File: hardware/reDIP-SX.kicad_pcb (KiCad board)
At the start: 6 copper layers, 17.8 x 40.6 mm, 130 parts, among them J1 DX07S016JA3, J10 Conn_01x01, J11 Conn_01x01, J2 Conn_01x01, J3 Conn_01x01, J4 Conn_01x01, J5 Conn_01x06, J6 Conn_01x06, J7 Conn_01x10, J8 Conn_01x10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

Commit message: Renamed to reDIP SX
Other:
- board text added: "reDIP SX"
- board text removed: "reDIP"
- board text removed: "sx"
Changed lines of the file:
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@@
   (general
     (thickness 1.6)
-    (drawings 99)
+    (drawings 98)
     (tracks 2870)
     (zones 0)
@@
   (page A4 portrait)
   (title_block
-    (title "reDIP sx")
+    (title "reDIP SX")
     (date 2021-01-17)
     (rev 0.1)
@@
       (effects (font (size 1 1) (thickness 0.15)))
     )
-    (fp_text user %R (at 0 0 45) (layer F.Fab)
-      (effects (font (size 0.2 0.2) (thickness 0.03)))
-    )
     (fp_line (start -0.71 0.51) (end -0.71 0.26) (layer F.SilkS) (width 0.12))
     (fp_line (start -0.71 0.51) (end -0.46 0.51) (layer F.SilkS) (width 0.12))
@@
     (fp_line (start 0.51 -0.31) (end 0.51 0.31) (layer F.Fab) (width 0.1))
     (fp_line (start -0.31 -0.31) (end 0.51 -0.31) (layer F.Fab) (width 0.1))
+    (fp_text user %R (at 0 0 45) (layer F.Fab)
+      (effects (font (size 0.2 0.2) (thickness 0.03)))
+    )
     (pad "" smd roundrect (at 0.35 0 45) (size 0.3 0.6) (layers F.Paste) (roundrect_rratio 0.125))
     (pad "" smd roundrect (at -0.35 0.225 45) (size 0.3 0.25) (layers F.Paste) (roundrect_rratio 0.2))
@@
       (effects (font (size 1 1) (thickness 0.15)))
     )
-    (fp_text user %R (at 0 0 45) (layer F.Fab)
-      (effects (font (size 0.5 0.5) (thickness 0.075)))
-    )
     (fp_line (start 1.5 1.1) (end 1.5 -1.1) (layer F.CrtYd) (width 0.05))
     (fp_line (start -1.5 -1.1) (end -1.5 1.1) (layer F.CrtYd) (width 0.05))
@@
     (fp_line (start 0.6 -0.9) (end -1.1 -0.9) (layer F.SilkS) (width 0.12))
     (fp_line (start -0.6 -0.5) (end -0.3 -0.8) (layer F.Fab) (width 0.1))
+    (fp_text user %R (at 0 0 45) (layer F.Fab)
+      (effects (font (size 0.5 0.5) (thickness 0.075)))
+    )
     (pad 6 smd roundrect (at 0.85 -0.5375 315) (size 0.5 0.375) (layers F.Cu F.Paste F.Mask) (roundrect_rratio 0.25)
       (net 88 /ESP_EN))
@@
       (effects (font (size 1 1) (thickness 0.15)))
     )
-    (fp_text user %R (at 0 0 90) (layer F.Fab)
-      (effects (font (size 0.3 0.3) (thickness 0.06)))
-    )
     (fp_line (start -0.5 0.975) (end 0.5 0.975) (layer F.Fab) (width 0.1))
     (fp_line (start 0.5 -0.975) (end 0.5 0.975) (layer F.Fab) (width 0.1))
@@
     (fp_line (start -0.75 1.175) (end 0.75 1.175) (layer F.CrtYd) (width 0.05))
     (fp_line (start -0.75 -1.175) (end -0.75 1.175) (layer F.CrtYd) (width 0.05))
+    (fp_text user %R (at 0 0 90) (layer F.Fab)
+      (effects (font (size 0.3 0.3) (thickness 0.06)))
+    )
     (pad 2 smd roundrect (at -0.3375 -0.25 270) (size 0.4 0.3) (layers F.Cu F.Paste F.Mask) (roundrect_rratio 0.2)
       (net 47 /ICE_POT_X))
@@
       (effects (font (size 1 1) (thickness 0.15)))
     )
-    (fp_text user %R (at 0 0 90) (layer F.Fab)
-      (effects (font (size 0.3 0.3) (thickness 0.06)))
-    )
     (fp_line (start -1 1.2) (end -1 -1.2) (layer F.CrtYd) (width 0.05))
     (fp_line (start 1 1.2) (end -1 1.2) (layer F.CrtYd) (width 0.05))
@@
     (fp_line (start -0.7 -0.55) (end -0.7 0.9) (layer F.Fab) (width 0.1))
     (fp_line (start -0.35 -0.9) (end -0.7 -0.55) (layer F.Fab) (width 0.1))
+    (fp_text user %R (at 0 0 90) (layer F.Fab)
+      (effects (font (size 0.3 0.3) (thickness 0.06)))
+    )
     (pad 10 smd roundrect (at -0.4 -0.7685 90) (size 0.225 0.563) (layers F.Cu F.Paste F.Mask) (roundrect_rratio 0.25)
       (net 72 /D+))
@@
       (effects (font (size 1 1) (thickness 0.15)))
     )
-    (fp_text user %R (at 0 0) (layer F.Fab)
-      (effects (font (size 0.3 0.3) (thickness 0.06)))
-    )
     (fp_line (start -0.7 -1.85) (end -0.4 -1.85) (layer F.SilkS) (width 0.12))
     (fp_line (start 0.4 -1.85) (end 0.7 -1.85) (layer F.SilkS) (width 0.12))
@@
     (fp_line (start -0.4 1.85) (end -0.7 1.85) (layer F.SilkS) (width 0.12))
     (fp_line (start -0.7 1.85) (end -0.7 1.65) (layer F.SilkS) (width 0.12))
+    (fp_text user %R (at 0 0) (layer F.Fab)
+      (effects (font (size 0.3 0.3) (thickness 0.06)))
+    )
     (pad 1 smd roundrect (at -0.35 -1.4 180) (size 0.25 0.5) (layers F.Cu F.Paste F.Mask) (roundrect_rratio 0.2)
       (net 70 /SBU1))
@@
       (effects (font (size 1 1) (thickness 0.15)))
     )
-    (fp_text user %R (at 0 0) (layer F.Fab)
-      (effects (font (size 0.7 0.7) (thickness 0.1)))
-    )
     (fp_line (start -1.6 -0.8) (end -0.8 -1.59) (layer F.Fab) (width 0.1))
     (fp_line (start -2.25 2.25) (end 2.25 2.25) (layer F.CrtYd) (width 0.05))
@@
     (fp_line (start -1.92 -1.91) (end -2.07 -2.06) (layer F.SilkS) (width 0.12))
     (fp_line (start -2.07 -2.06) (end -1.45 -2.06) (layer F.SilkS) (width 0.12))
+    (fp_text user %R (at 0 0) (layer F.Fab)
+      (effects (font (size 0.7 0.7) (thickness 0.1)))
+    )
     (pad 1 smd roundrect (at -1.075 -1.075) (size 1.35 1.35) (layers F.Cu F.Paste F.Mask) (roundrect_rratio 0.05)
       (net 1 "Net-(AE1-Pad1)"))
@@
       (effects (font (size 1 1) (thickness 0.15)))
     )
-    (fp_text user %R (at 0 0 90) (layer F.Fab)
-      (effects (font (size 0.2 0.2) (thickness 0.04)))
-    )
     (fp_line (start -0.68 -0.68) (end -0.43 -0.68) (layer F.SilkS) (width 0.12))
     (fp_line (start 0.68 -0.43) (end 0.68 -0.68) (layer F.SilkS) (width 0.12))
@@
     (fp_line (start -0.75 0.75) (end 0.75 0.75) (layer F.CrtYd) (width 0.05))
     (fp_line (start -0.75 -0.75) (end 0.75 -0.75) (layer F.CrtYd) (width 0.05))
+    (fp_text user %R (at 0 0 90) (layer F.Fab)
+      (effects (font (size 0.2 0.2) (thickness 0.04)))
+    )
     (pad C3 smd circle (at 0.4 0.4 90) (size 0.2 0.2) (layers F.Cu F.Paste F.Mask)
       (net 2 GND))
@@
     (effects (font (size 1.1 1.1) (thickness 0.15)) (justify mirror))
   )
-  (gr_text sx (at 113.31 120.02 270) (layer F.SilkS)
-    (effects (font (size 1 1) (thickness 0.2)))
-  )
   (gr_text "© 2021" (at 102.6 125.51 90) (layer B.SilkS)
     (effects (font (size 0.8 0.8) (thickness 0.15)) (justify mirror))
@@
     (effects (font (size 0.8 0.8) (thickness 0.15)) (justify mirror))
   )
-  (gr_text reDIP (at 113.31 116.81 270) (layer F.SilkS)
+  (gr_text "reDIP SX" (at 113.32 117.63 -90) (layer F.SilkS)
     (effects (font (size 1 1) (thickness 0.2)))
   )

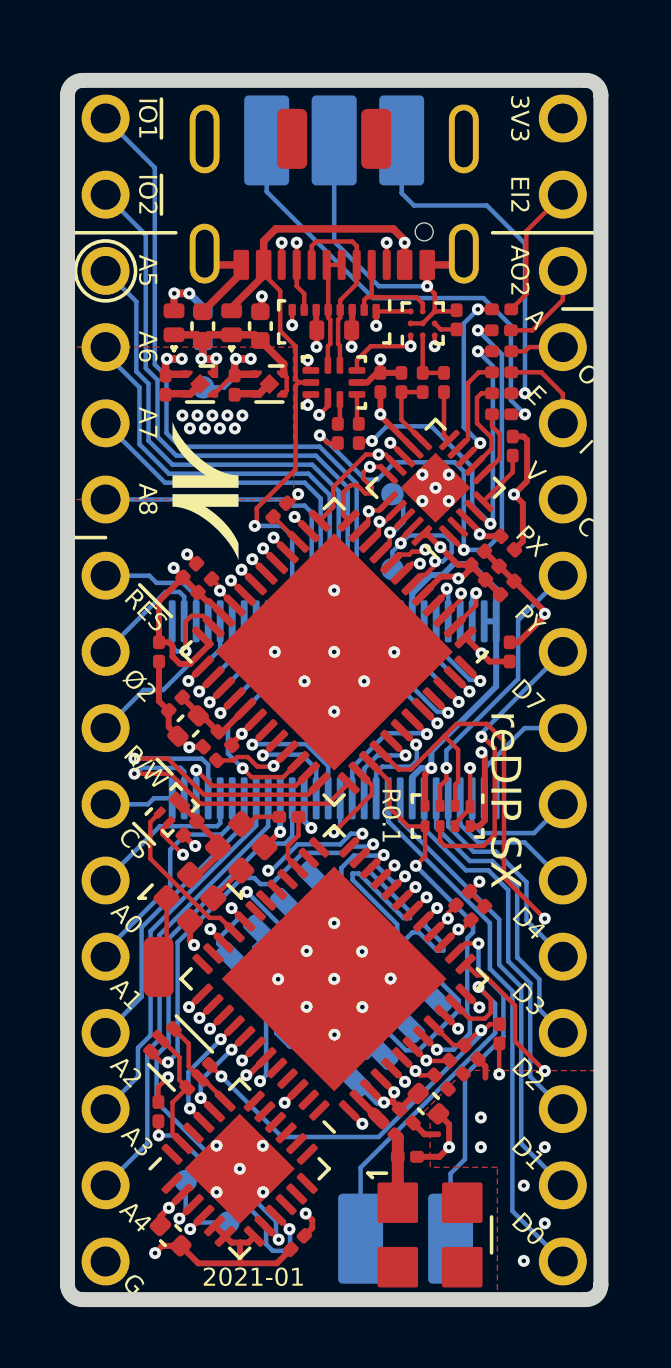
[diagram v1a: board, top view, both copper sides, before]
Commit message: Adjusted TVSOP-56 footprint to match datasheet
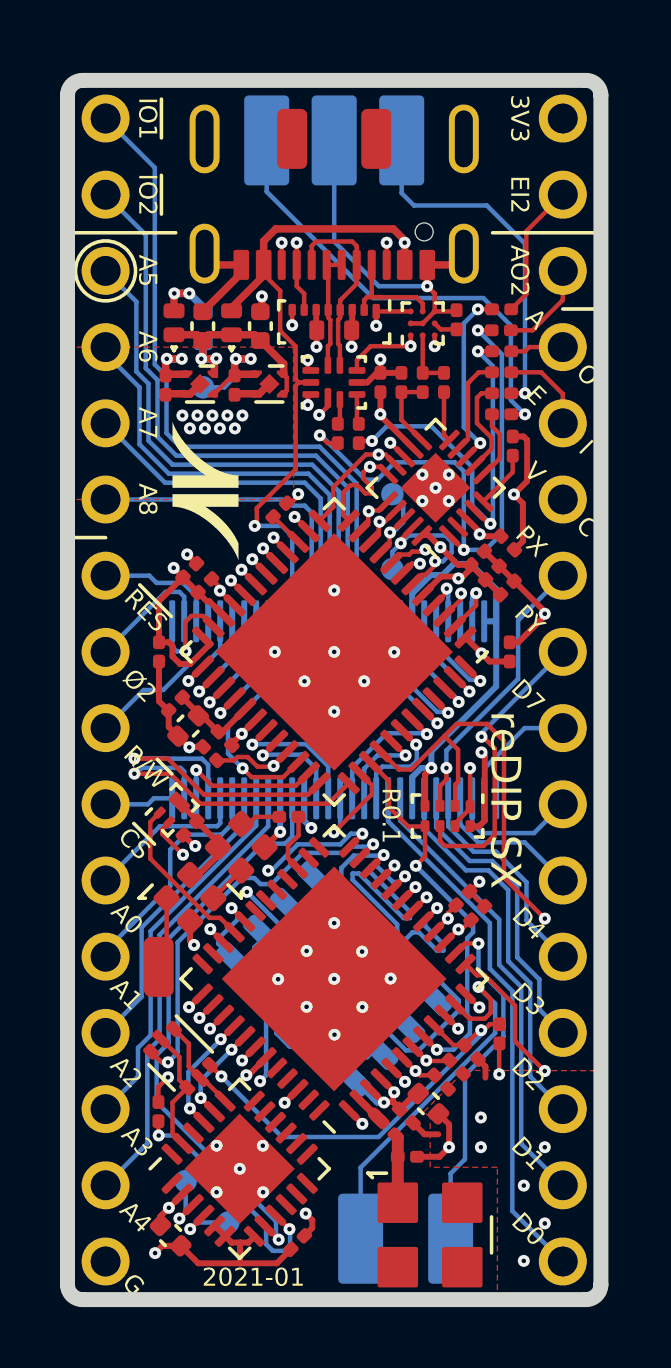
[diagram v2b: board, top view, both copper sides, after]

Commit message: Various fixes
* Added 10k pullup for SPI SCLK, following iCE40 Hardware Checklist
* Increased through hole pad sizes for USB-C connector
* Increased courtyard for TVSOP-56 footprint
* Changed VCC to power symbol
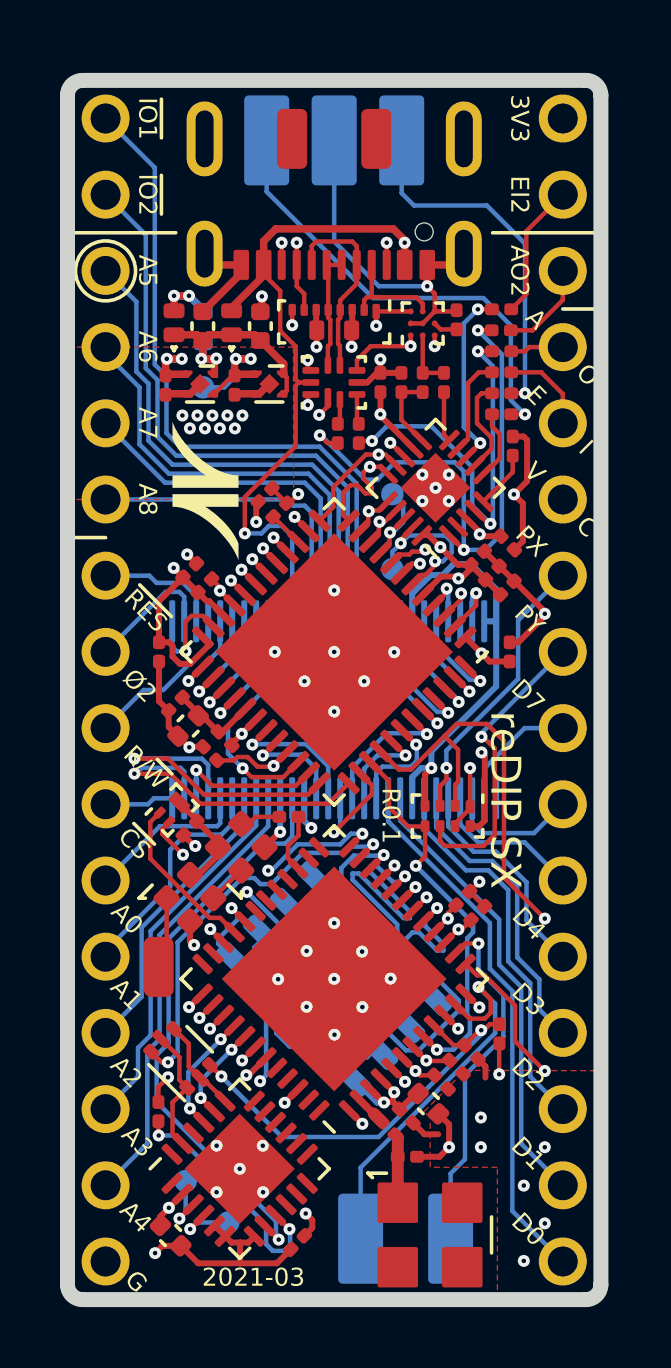
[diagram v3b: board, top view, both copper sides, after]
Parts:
- added R10: 10k, Resistor_SMD:R_0201_0603Metric, F.Cu at (105.3, 107.5)
- J1: value DX07S016JA3 -> DX07S016JA1
- turned Q1 to 135 degrees
- renumbered R10 to R11, R11 to R12, R12 to R13, U11 to U10, U10 to U11
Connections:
- net /Vcc renamed VCC
- Q1 pad 1: /RTS -> /DTR
- Q1 pad 2: /DTR -> /RTS
- Q1 pad 3: /SYS_CLK -> /ESP_EN
- Q1 pad 4: /DTR -> /RTS
- Q1 pad 5: /RTS -> /DTR
- Q1 pad 6: /ESP_EN -> /SYS_CLK
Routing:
- net VBUS: track 28.4 -> 29.3 mm
- net /SPI_SCLK: track 30.6 -> 31.3 mm
- net +3V3: track 68.1 -> 68.8 mm, vias 21 -> 22
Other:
- board text added: "2021-03"
- board text removed: "2021-01"

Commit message: Replaced non-stocked parts
* Replaced 2 bit bus switch and 1.2V LDO with more readily available parts
* Length matching for SPI_SIO3 (note that length matching is probably uncalled-for)
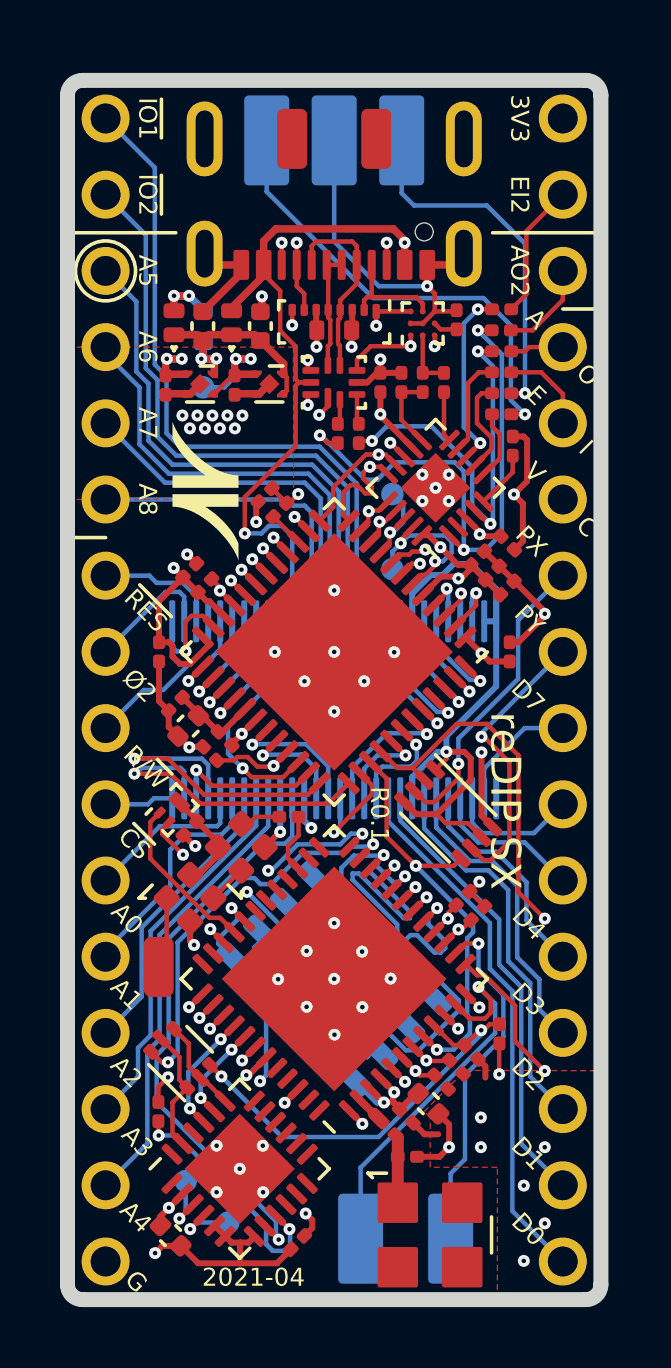
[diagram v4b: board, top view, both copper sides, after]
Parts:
- U1: value NCP163AMX120TBG -> NCP115AMX120TCG; footprint ONSemi:CASE711AJ_1.0x1.0mm_P0.65mm -> ONSemi:CASE_711AJ_1.0x1.0mm_P0.65mm
- U11: value CBTD3306GT -> 7WBD3306USG; footprint Nexperia:SOT-833-1 -> ONSemi:CASE_493-8_2.3x2mm_P0.5mm
- U2: footprint ONSemi:CASE711AJ_1.0x1.0mm_P0.65mm -> ONSemi:CASE_711AJ_1.0x1.0mm_P0.65mm
- U3: footprint ONSemi:523BC_1.4x1.8_P0.4mm -> ONSemi:CASE_523BC_1.4x1.8_P0.4mm
- moved U11 0.06 mm to (111.4, 118.1), turned to 315 degrees
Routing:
- net GND: track 65.2 -> 68.7 mm, vias 57 -> 56
- net /ICE_POT_X: track 24.4 -> 22.4 mm
- net /SPI_SIO3: track 32.7 -> 31.6 mm
- net /ICE_POT_Y: track 13.2 -> 14.2 mm
- net /POT_X: track 9.37 -> 10.2 mm
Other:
- board text added: "2021-04"
- board text removed: "2021-03"

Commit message: Various improvements
* Improved decoupling and PLL power filtering,
  following suggestions by @smunaut for reDIP-SID
* Capped component position resolution to 0.01mm
* Routing cleanups
* Note on the iCE40 PLL output-only-pin trap in the schematic
* Added note on pin-in-paste for USB-C connector
* Moved KiCost BOM spreadsheet to documentation/
* Files for fabrication and assembly generated by KiKit
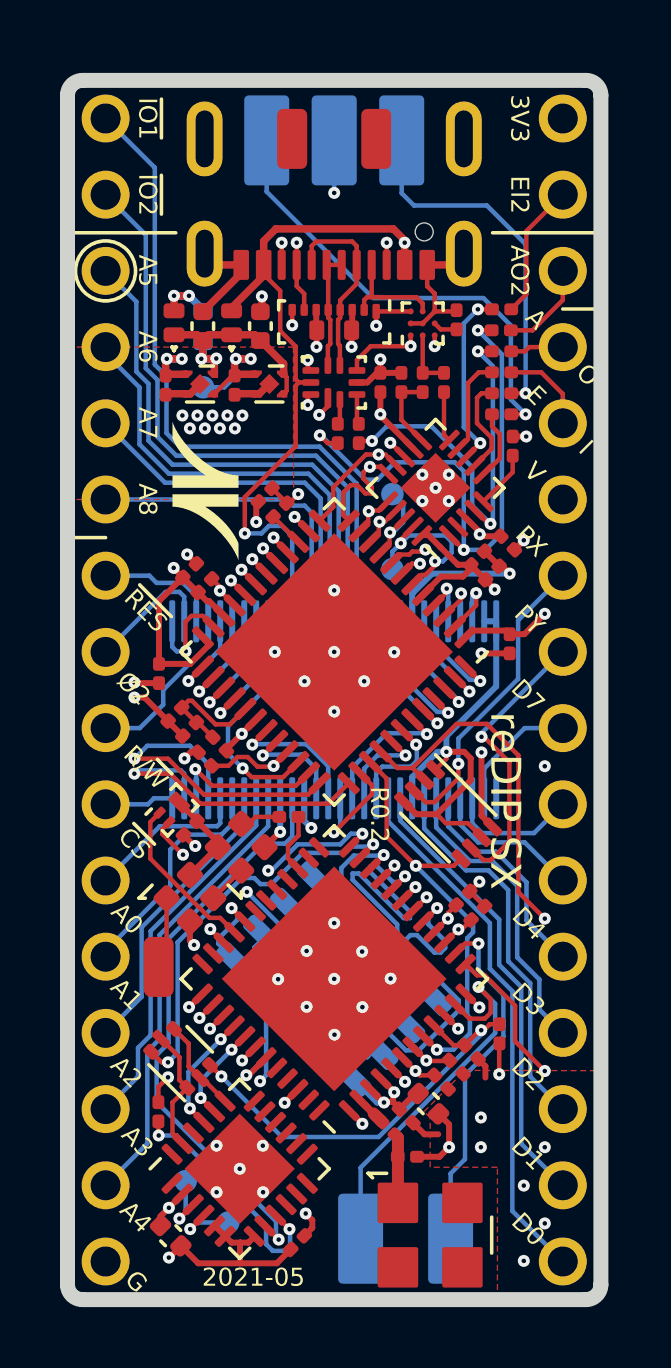
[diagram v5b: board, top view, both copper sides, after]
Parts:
- removed the C26 at (113.4, 110.6)
- removed the C29 at (102.8, 115.2)
- removed the C31 at (103.5, 116.1)
- added C28: 1uF, Capacitor_SMD:C_0201_0603Metric, F.Cu at (102.8, 115.3)
- added C30: 0.1uF, Capacitor_SMD:C_0201_0603Metric, F.Cu at (103.3, 116.3)
- moved C26 0.72 mm to (101.8, 113.4)
- moved C24 0.70 mm to (112.9, 110.1)
- moved C25 0.70 mm to (112.4, 109.6)
- moved C27 0.34 mm to (102.3, 114.8)
- moved C32 0.27 mm to (113.5, 112.4), turned to 270 degrees
- moved R9 0.25 mm to (103.8, 115.8)
- renumbered C27 to C26, C28 to C27, C30 to C29, C32 to C31, C33 to C32
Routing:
- net GND: track 68.7 -> 56.3 mm, vias 56 -> 61
- net +1V2: track 33.2 -> 34.5 mm, vias 5 -> 4
- net Net-(C27-Pad1): track 2.94 -> 4.21 mm
- net +3V3: track 68.8 -> 70.0 mm
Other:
- board text added: "2021-05"
- board text added: "R0.2"
- board text removed: "2021-04"
- board text removed: "C"
- board text removed: "R0.1"

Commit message: Reduced layer count from 6 to 4
As originally suggested by @smunaut for reDIP SID.
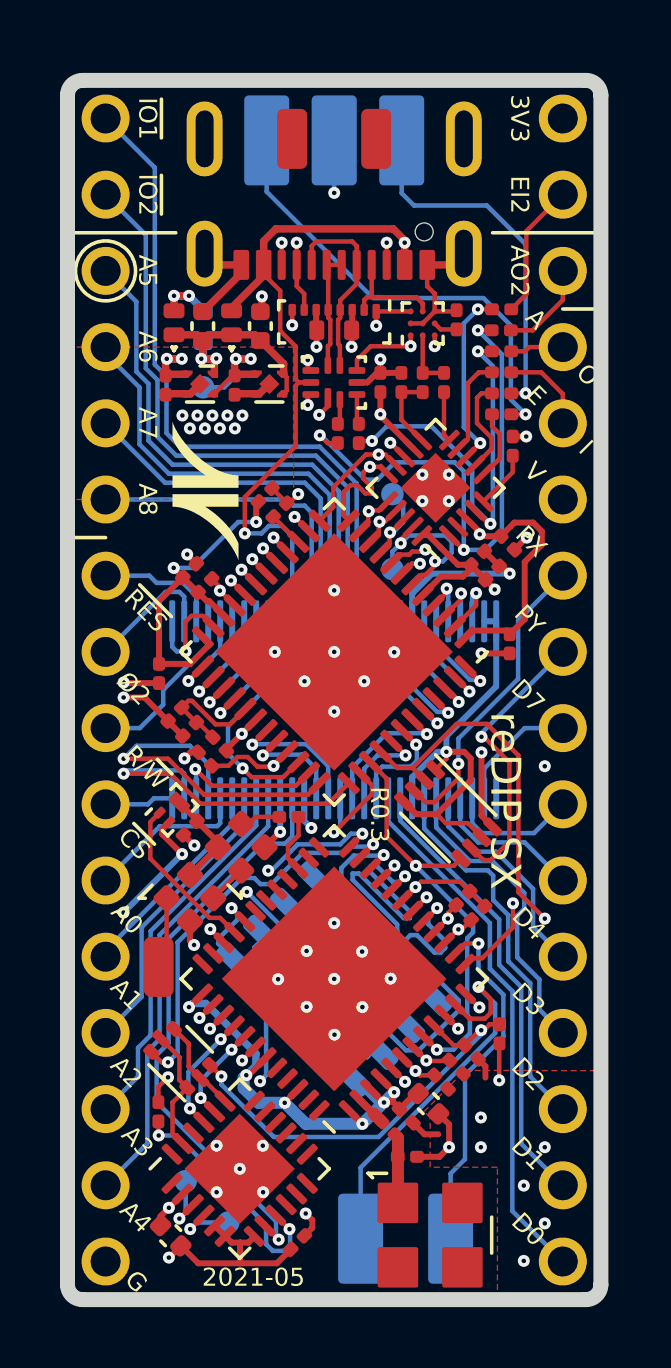
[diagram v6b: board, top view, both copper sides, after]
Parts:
- removed the SolderMask D0.45mm at (111.0, 107.2)
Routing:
- net /A_SEL: track 51.7 -> 25.5 mm
- net +3V3: track 70.0 -> 65.5 mm, vias 22 -> 21
- net GND: track 56.3 -> 57.1 mm, vias 61 -> 60
- net /CC2: track 37.8 -> 38.5 mm
- net /ICE_Ø2: track 10.4 -> 11.1 mm
- net /ICE_R_~W~: track 10.9 -> 11.6 mm
- net /A1: track 7.73 -> 7.03 mm
- net /I2S_DIN: track 36.5 -> 35.9 mm
- net /I2S_WCLK: track 39.7 -> 39.1 mm
- net /ICE_POT_X: track 22.4 -> 21.8 mm
- added copper zone on In2.Cu, net +3V3
- added copper zone on In1.Cu, net VBUS
- added copper zone on In2.Cu, net VCC
- removed copper zone on In3.Cu, net +1V2
- removed copper zone on In3.Cu, net +3V3
- removed copper zone on In3.Cu, net GND
- removed copper zone on In4.Cu, net GND
- removed copper zone on In3.Cu, net VBUS
- removed copper zone on In3.Cu, net VCC
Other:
- copper layers 6 -> 4
- board text added: "R0.3"
- board text removed: "R0.2"
